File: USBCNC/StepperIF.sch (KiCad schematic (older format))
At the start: 0 parts

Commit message: Added Pololu module interface
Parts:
- added U?: DRV8825, symbol DRV8825
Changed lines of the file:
@@
 LIBS:DRV8825
 LIBS:motordriver
+LIBS:USBCNC-cache
 EELAYER 25 0
 EELAYER END
 $Descr A4 11693 8268
 encoding utf-8
-Sheet 1 5
+Sheet 4 5
 Title ""
 Date ""
@@
 Comment4 ""
 $EndDescr
+$Comp
+L DRV8825 U?
+U 1 1 55A0FB70
+P 3800 2200
+F 0 "U?" H 3600 2850 60  0000 C CNN
+F 1 "DRV8825" H 3750 2100 60  0000 C CNN
+F 2 "" H 3800 2200 60  0000 C CNN
+F 3 "" H 3800 2200 60  0000 C CNN
+	1    3800 2200
+	1    0    0    -1
+$EndComp
 $EndSCHEMATC

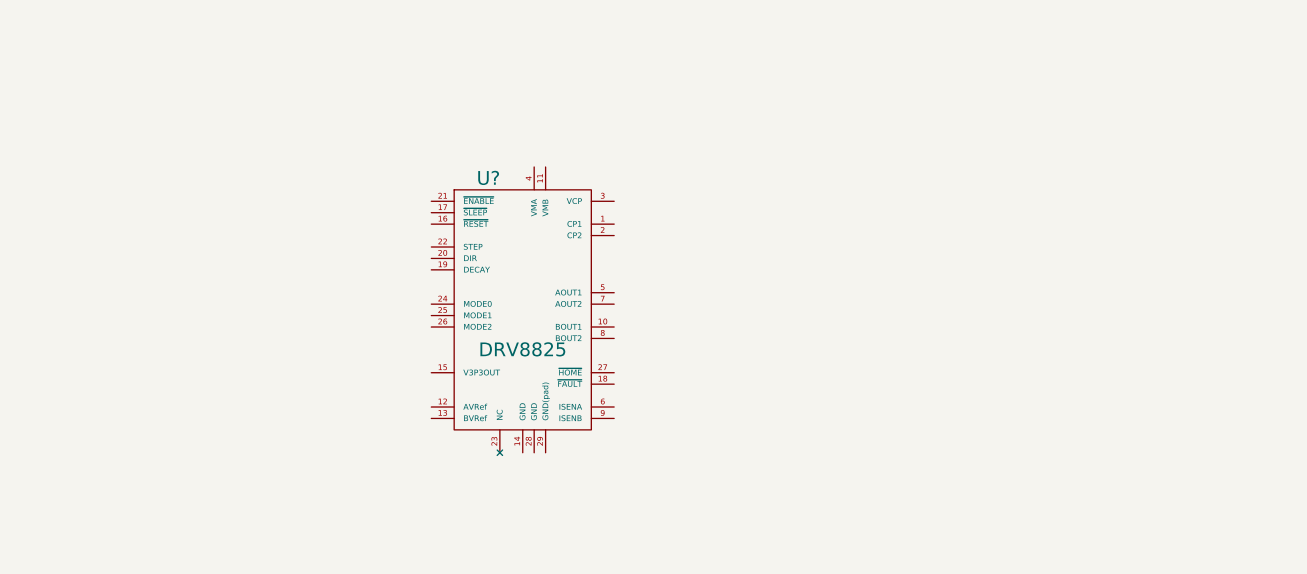
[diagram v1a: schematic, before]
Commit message: Added components for one  on board stepper driver
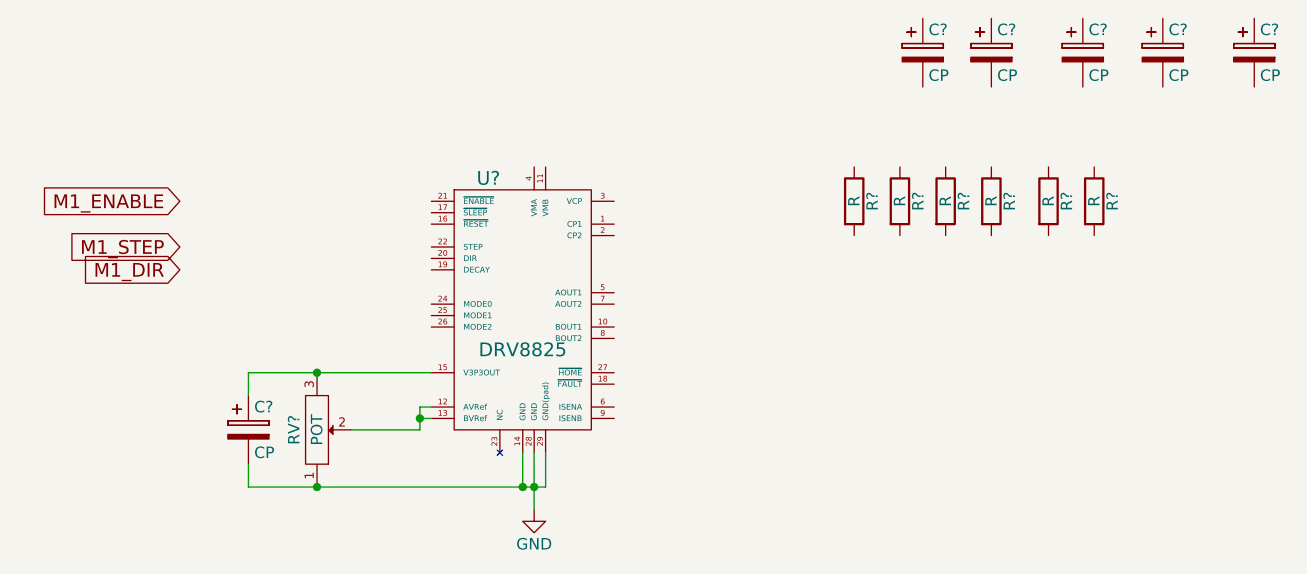
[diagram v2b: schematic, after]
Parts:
- added C? (x6): CP, symbol CP
- added R? (x6): R, symbol R
- added RV?: POT, symbol POT
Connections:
- net at U?.12 (AVRef): now also U?.13 (BVRef), RV?.2
- net GND: now reaches U?.14 (GND)
- net GND: now also U?.28 (GND), U?.29 (GND(pad)), C?.2, RV?.1
- net at U?.15 (V3P3OUT): now also C?.1, RV?.3
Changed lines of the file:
@@
 	1    0    0    -1
 $EndComp
+$Comp
+L GND #PWR?
+U 1 1 55A3C802
+P 3800 3000
+F 0 "#PWR?" H 3800 2750 50  0001 C CNN
+F 1 "GND" H 3800 2850 50  0000 C CNN
+F 2 "" H 3800 3000 60  0000 C CNN
+F 3 "" H 3800 3000 60  0000 C CNN
+	1    3800 3000
+	1    0    0    -1
+$EndComp
+$Comp
+L POT RV?
+U 1 1 55A3C933
+P 2850 2650
+F 0 "RV?" H 2850 2550 50  0000 C CNN
+F 1 "POT" H 2850 2650 50  0000 C CNN
+F 2 "" H 2850 2650 60  0000 C CNN
+F 3 "" H 2850 2650 60  0000 C CNN
+	1    2850 2650
+	0    1    -1   0
+$EndComp
+Wire Wire Line
+	2550 2400 3350 2400
+Wire Wire Line
+	2550 2900 3850 2900
+Wire Wire Line
+	3800 2750 3800 3000
+Connection ~ 3800 2900
+Wire Wire Line
+	3750 2750 3750 2900
+Connection ~ 3750 2900
+Wire Wire Line
+	3850 2900 3850 2750
+Wire Wire Line
+	3350 2550 3300 2550
+Wire Wire Line
+	3300 2550 3300 2650
+Wire Wire Line
+	3300 2600 3350 2600
+Wire Wire Line
+	3300 2650 3000 2650
+Connection ~ 3300 2600
+$Comp
+L CP C?
+U 1 1 55A3CAF9
+P 2550 2650
+F 0 "C?" H 2575 2750 50  0000 L CNN
+F 1 "CP" H 2575 2550 50  0000 L CNN
+F 2 "" H 2588 2500 30  0000 C CNN
+F 3 "" H 2550 2650 60  0000 C CNN
+	1    2550 2650
+	1    0    0    -1
+$EndComp
+Wire Wire Line
+	2550 2800 2550 2900
+Connection ~ 2850 2900
+Wire Wire Line
+	2550 2400 2550 2500
+Connection ~ 2850 2400
+$Comp
+L CP C?
+U 1 1 55A3CBC1
+P 6950 1000
+F 0 "C?" H 6975 1100 50  0000 L CNN
+F 1 "CP" H 6975 900 50  0000 L CNN
+F 2 "" H 6988 850 30  0000 C CNN
+F 3 "" H 6950 1000 60  0000 C CNN
+	1    6950 1000
+	1    0    0    -1
+$EndComp
+$Comp
+L CP C?
+U 1 1 55A3CC02
+P 6550 1000
+F 0 "C?" H 6575 1100 50  0000 L CNN
+F 1 "CP" H 6575 900 50  0000 L CNN
+F 2 "" H 6588 850 30  0000 C CNN
+F 3 "" H 6550 1000 60  0000 C CNN
+	1    6550 1000
+	1    0    0    -1
+$EndComp
+$Comp
+L CP C?
+U 1 1 55A3CC68
+P 6200 1000
+F 0 "C?" H 6225 1100 50  0000 L CNN
+F 1 "CP" H 6225 900 50  0000 L CNN
+F 2 "" H 6238 850 30  0000 C CNN
+F 3 "" H 6200 1000 60  0000 C CNN
+	1    6200 1000
+	1    0    0    -1
+$EndComp
+$Comp
+L CP C?
+U 1 1 55A3CC6E
+P 5800 1000
+F 0 "C?" H 5825 1100 50  0000 L CNN
+F 1 "CP" H 5825 900 50  0000 L CNN
+F 2 "" H 5838 850 30  0000 C CNN
+F 3 "" H 5800 1000 60  0000 C CNN
+	1    5800 1000
+	1    0    0    -1
+$EndComp
+$Comp
+L CP C?
+U 1 1 55A3CCA3
+P 5500 1000
+F 0 "C?" H 5525 1100 50  0000 L CNN
+F 1 "CP" H 5525 900 50  0000 L CNN
+F 2 "" H 5538 850 30  0000 C CNN
+F 3 "" H 5500 1000 60  0000 C CNN
+	1    5500 1000
+	1    0    0    -1
+$EndComp
+$Comp
+L R R?
+U 1 1 55A3D0B4
+P 5200 1650
+F 0 "R?" V 5280 1650 50  0000 C CNN
+F 1 "R" V 5200 1650 50  0000 C CNN
+F 2 "" V 5130 1650 30  0000 C CNN
+F 3 "" H 5200 1650 30  0000 C CNN
+	1    5200 1650
+	1    0    0    -1
+$EndComp
+$Comp
+L R R?
+U 1 1 55A3D135
+P 5400 1650
+F 0 "R?" V 5480 1650 50  0000 C CNN
+F 1 "R" V 5400 1650 50  0000 C CNN
+F 2 "" V 5330 1650 30  0000 C CNN
+F 3 "" H 5400 1650 30  0000 C CNN
+	1    5400 1650
+	1    0    0    -1
+$EndComp
+$Comp
+L R R?
+U 1 1 55A3D181
+P 5600 1650
+F 0 "R?" V 5680 1650 50  0000 C CNN
+F 1 "R" V 5600 1650 50  0000 C CNN
+F 2 "" V 5530 1650 30  0000 C CNN
+F 3 "" H 5600 1650 30  0000 C CNN
+	1    5600 1650
+	1    0    0    -1
+$EndComp
+$Comp
+L R R?
+U 1 1 55A3D187
+P 5800 1650
+F 0 "R?" V 5880 1650 50  0000 C CNN
+F 1 "R" V 5800 1650 50  0000 C CNN
+F 2 "" V 5730 1650 30  0000 C CNN
+F 3 "" H 5800 1650 30  0000 C CNN
+	1    5800 1650
+	1    0    0    -1
+$EndComp
+$Comp
+L R R?
+U 1 1 55A3D203
+P 6050 1650
+F 0 "R?" V 6130 1650 50  0000 C CNN
+F 1 "R" V 6050 1650 50  0000 C CNN
+F 2 "" V 5980 1650 30  0000 C CNN
+F 3 "" H 6050 1650 30  0000 C CNN
+	1    6050 1650
+	1    0    0    -1
+$EndComp
+$Comp
+L R R?
+U 1 1 55A3D209
+P 6250 1650
+F 0 "R?" V 6330 1650 50  0000 C CNN
+F 1 "R" V 6250 1650 50  0000 C CNN
+F 2 "" V 6180 1650 30  0000 C CNN
+F 3 "" H 6250 1650 30  0000 C CNN
+	1    6250 1650
+	1    0    0    -1
+$EndComp
+Text GLabel 2250 1650 0    60   Input ~ 0
+M1_ENABLE
+Text GLabel 2250 1850 0    60   Input ~ 0
+M1_STEP
+Text GLabel 2250 1950 0    60   Input ~ 0
+M1_DIR
 $EndSCHEMATC

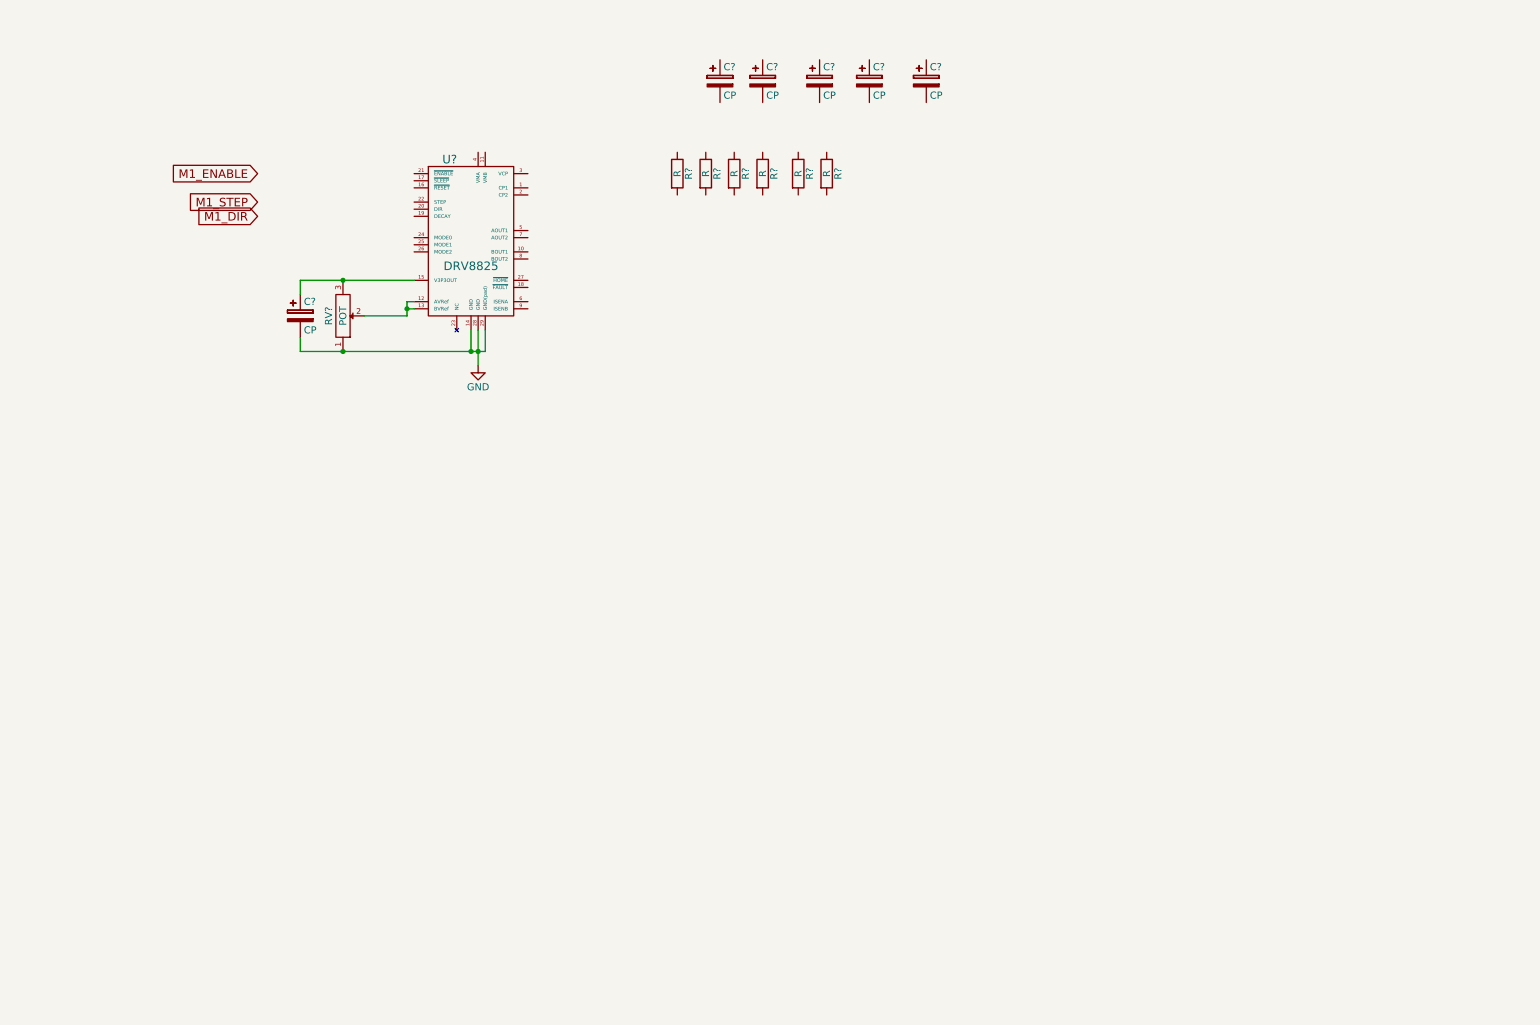
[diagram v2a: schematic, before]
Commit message: Completed the DRV8825 Block(s), and reorganized the pololu blocks
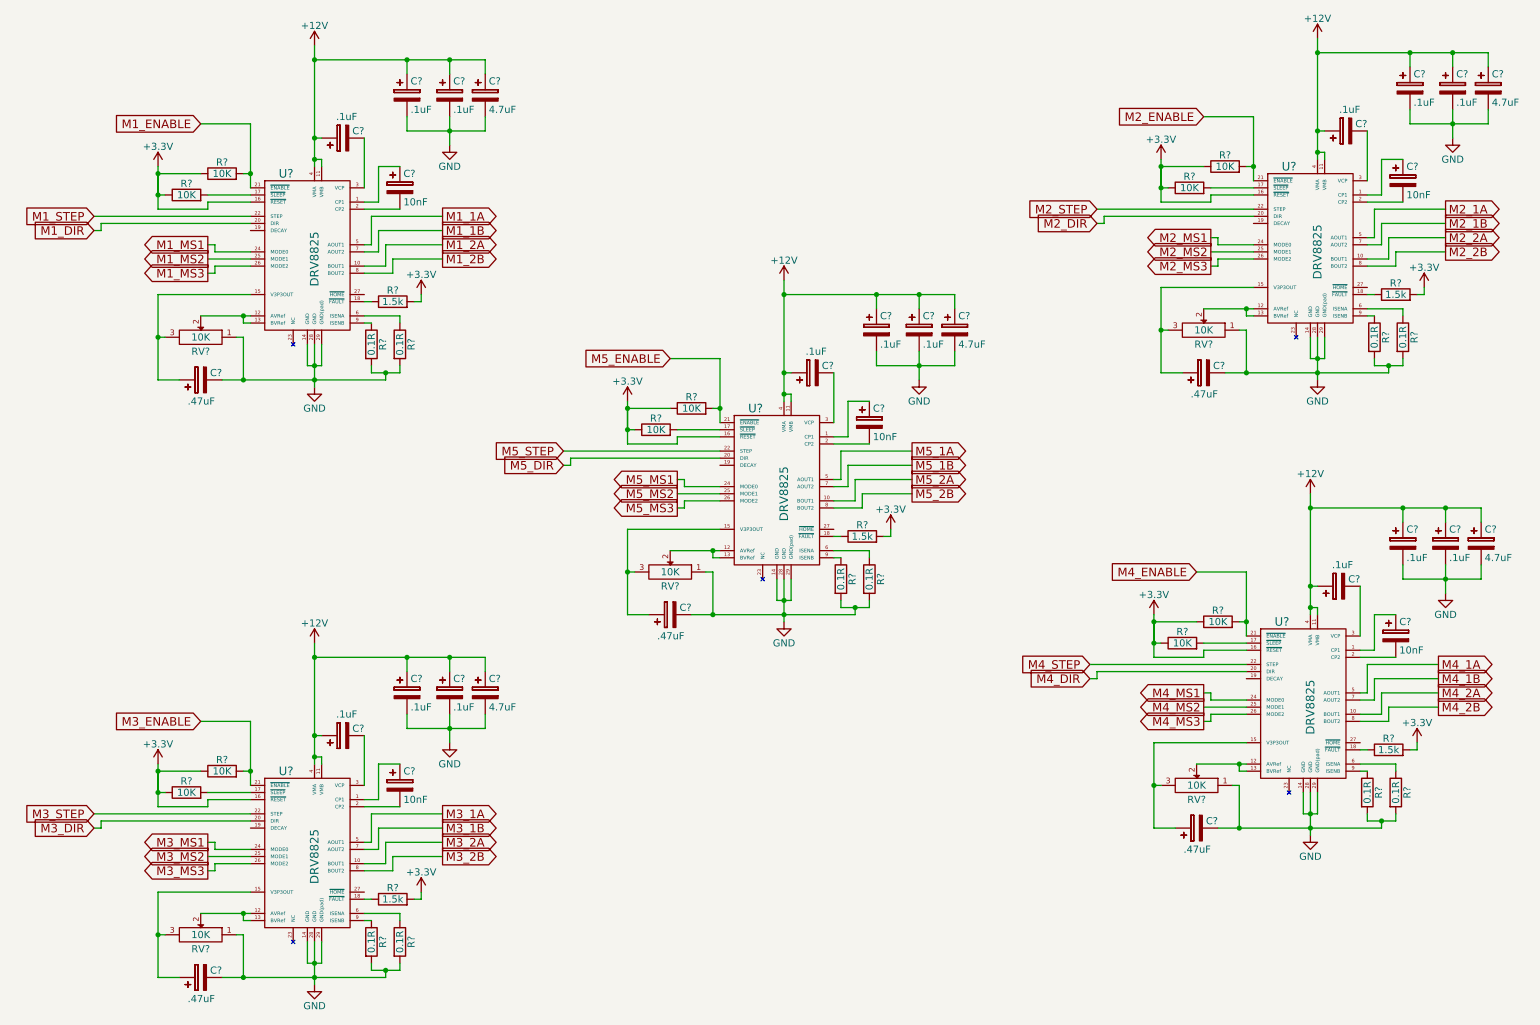
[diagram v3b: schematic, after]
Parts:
- removed C? (x6): CP, symbol CP
- removed R? (x5): R, symbol R
- removed RV?: POT, symbol POT
- removed U?: DRV8825, symbol DRV8825
- added C? (x15): .1uF, symbol CP
- added C? (x5): 10nF, symbol CP
- added C? (x5): .47uF, symbol CP
- added C? (x5): 4.7uF, symbol CP
- added R? (x10): 10K, symbol R
- added R? (x10): 0.1R, symbol R
- added R? (x4): 1.5k, symbol R
- added RV? (x5): 10K, symbol POT
- added U? (x5): DRV8825, symbol DRV8825
- R?: value R -> 1.5k
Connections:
- net GND: now also C?.2, C?.2, C?.2, C?.2, C?.2, C?.2, C?.2, C?.2, C?.2, C?.2, C?.2, C?.2, C?.2, C?.2, C?.2, C?.2, C?.2, C?.2, C?.2, C?.2, R?.2, R?.2, R?.2, R?.2, R?.2, R?.2, R?.2, R?.2, R?.2, R?.2, RV?.1, RV?.1, RV?.1, RV?.1, RV?.1, U?.14 (GND), U?.14 (GND), U?.14 (GND), U?.14 (GND), U?.14 (GND), U?.28 (GND), U?.28 (GND), U?.28 (GND), U?.28 (GND), U?.28 (GND), U?.29 (GND(pad)), U?.29 (GND(pad)), U?.29 (GND(pad)), U?.29 (GND(pad)), U?.29 (GND(pad))
- net M1_DIR: now also U?.20 (DIR)
- net M1_ENABLE: now also R?.2, U?.21 (~ENABLE)
- net M1_STEP: now also U?.22 (STEP)
- net at R?.1: now also U?.18 (~FAULT)
- net +3V3: now reaches R?.2
- net +3V3: now also R?.1, R?.1, R?.1, R?.1, R?.1, R?.1, R?.1, R?.1, R?.1, R?.1, R?.2, R?.2, R?.2, R?.2, U?.16 (~RESET), U?.16 (~RESET), U?.16 (~RESET), U?.16 (~RESET), U?.16 (~RESET)
- new net: C?.1, U?.1 (CP1) (x5)
- new net: RV?.2, U?.12 (AVRef), U?.13 (BVRef) (x5)
- new net: C?.1, RV?.3, U?.15 (V3P3OUT) (x5)
- new net: R?.2, U?.17 (~SLEEP) (x5)
- new net: C?.2, U?.2 (CP2) (x5)
- new net: C?.2, U?.3 (VCP) (x5)
- new net: R?.1, U?.6 (ISENA) (x5)
- new net: R?.1, U?.9 (ISENB) (x5)
- new net: R?.1, U?.18 (~FAULT) (x4)
- new net +12V: C?.1, C?.1, C?.1, C?.1, C?.1, C?.1, C?.1, C?.1, C?.1, C?.1, C?.1, C?.1, C?.1, C?.1, C?.1, C?.1, C?.1, C?.1, C?.1, C?.1, U?.11 (VMB), U?.11 (VMB), U?.11 (VMB), U?.11 (VMB), U?.11 (VMB), U?.4 (VMA), U?.4 (VMA), U?.4 (VMA), U?.4 (VMA), U?.4 (VMA)
- new net M1_1A: U?.5 (AOUT1)
- new net M1_1B: U?.7 (AOUT2)
- new net M1_2A: U?.10 (BOUT1)
- new net M1_2B: U?.8 (BOUT2)
- new net M1_MS1: U?.24 (MODE0)
- new net M1_MS2: U?.25 (MODE1)
- new net M1_MS3: U?.26 (MODE2)
- new net M2_1A: U?.5 (AOUT1)
- new net M2_1B: U?.7 (AOUT2)
- new net M2_2A: U?.10 (BOUT1)
- new net M2_2B: U?.8 (BOUT2)
- new net M2_DIR: U?.20 (DIR)
- new net M2_ENABLE: R?.2, U?.21 (~ENABLE)
- new net M2_MS1: U?.24 (MODE0)
- new net M2_MS2: U?.25 (MODE1)
- new net M2_MS3: U?.26 (MODE2)
- new net M2_STEP: U?.22 (STEP)
- new net M3_1A: U?.5 (AOUT1)
- new net M3_1B: U?.7 (AOUT2)
- new net M3_2A: U?.10 (BOUT1)
- new net M3_2B: U?.8 (BOUT2)
- new net M3_DIR: U?.20 (DIR)
- new net M3_ENABLE: R?.2, U?.21 (~ENABLE)
- new net M3_MS1: U?.24 (MODE0)
- new net M3_MS2: U?.25 (MODE1)
- new net M3_MS3: U?.26 (MODE2)
- new net M3_STEP: U?.22 (STEP)
- new net M4_1A: U?.5 (AOUT1)
- new net M4_1B: U?.7 (AOUT2)
- new net M4_2A: U?.10 (BOUT1)
- new net M4_2B: U?.8 (BOUT2)
- new net M4_DIR: U?.20 (DIR)
- new net M4_ENABLE: R?.2, U?.21 (~ENABLE)
- new net M4_MS1: U?.24 (MODE0)
- new net M4_MS2: U?.25 (MODE1)
- new net M4_MS3: U?.26 (MODE2)
- new net M4_STEP: U?.22 (STEP)
- new net M5_1A: U?.5 (AOUT1)
- new net M5_1B: U?.7 (AOUT2)
- new net M5_2A: U?.10 (BOUT1)
- new net M5_2B: U?.8 (BOUT2)
- new net M5_DIR: U?.20 (DIR)
- new net M5_ENABLE: R?.2, U?.21 (~ENABLE)
- new net M5_MS1: U?.24 (MODE0)
- new net M5_MS2: U?.25 (MODE1)
- new net M5_MS3: U?.26 (MODE2)
- new net M5_STEP: U?.22 (STEP)
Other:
- moved on the sheet: R?

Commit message: Fixing ERC
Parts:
- gave numbers to parts that had none: 65
